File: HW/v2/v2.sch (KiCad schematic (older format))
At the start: 19 parts, among them J1 Encoder and LCD interface, J2 Fan_conn, J3 SDcardHeader, J4 OUT2, J5 OUT2, Q1 BC847, Q2 BC847, Q3 IRF7341, U1 LM75

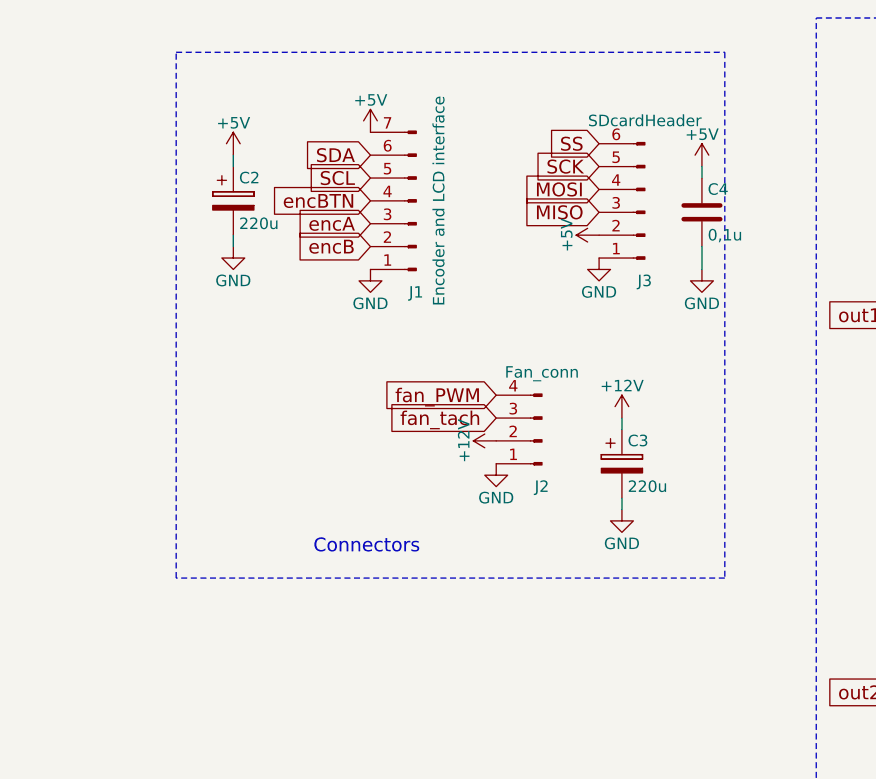
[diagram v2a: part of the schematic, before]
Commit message: i2c pots for calibrating
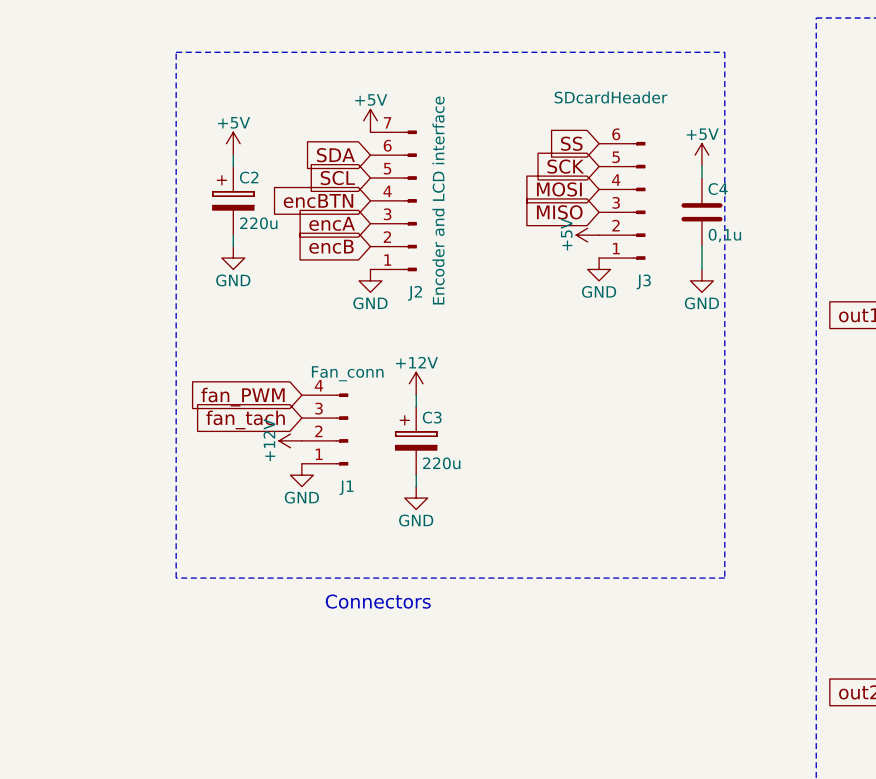
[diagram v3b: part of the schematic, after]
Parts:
- renumbered J2 to J1, J1 to J2
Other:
- moved on the sheet: C3, J1
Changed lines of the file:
@@
 encB
 $Comp
-L Conn_01x07_Male J1
+L Conn_01x07_Male J2
 U 1 1 5AD8A8D0
 P 6400 1600
-F 0 "J1" H 6400 2000 50  0000 C CNN
+F 0 "J2" H 6400 2000 50  0000 C CNN
 F 1 "Encoder and LCD interface" V 6300 1600 50  0000 C CNN
 F 2 "Pin_Headers:Pin_Header_Straight_1x07_Pitch2.54mm" H 6400 1600 50  0001 C CNN
@@
 	9950 3200 9950 3100
 Connection ~ 10250 3100
-Text GLabel 6750 2450 0    60   Input ~ 0
+Text GLabel 5900 2450 0    60   Input ~ 0
 fan_PWM
 $Comp
-L Conn_01x04_Male J2
+L Conn_01x04_Male J1
 U 1 1 5ADA285E
-P 6950 2650
-F 0 "J2" H 6950 2850 50  0000 C CNN
-F 1 "Fan_conn" H 6950 2350 50  0000 C CNN
-F 2 "Pin_Headers:Pin_Header_Straight_1x04_Pitch2.54mm" H 6950 2650 50  0001 C CNN
-F 3 "" H 6950 2650 50  0001 C CNN
-	1    6950 2650
+P 6100 2650
+F 0 "J1" H 6100 2850 50  0000 C CNN
+F 1 "Fan_conn" H 6100 2350 50  0000 C CNN
+F 2 "Pin_Headers:Pin_Header_Straight_1x04_Pitch2.54mm" H 6100 2650 50  0001 C CNN
+F 3 "" H 6100 2650 50  0001 C CNN
+	1    6100 2650
 	-1   0    0    1
 $EndComp
@@
 L +12V #PWR016
 U 1 1 5ADA2B19
-P 6750 2650
-F 0 "#PWR016" H 6750 2500 50  0001 C CNN
-F 1 "+12V" H 6750 2790 50  0000 C CNN
-F 2 "" H 6750 2650 50  0001 C CNN
-F 3 "" H 6750 2650 50  0001 C CNN
-	1    6750 2650
+P 5900 2650
+F 0 "#PWR016" H 5900 2500 50  0001 C CNN
+F 1 "+12V" H 5900 2790 50  0000 C CNN
+F 2 "" H 5900 2650 50  0001 C CNN
+F 3 "" H 5900 2650 50  0001 C CNN
+	1    5900 2650
 	0    -1   -1   0
 $EndComp
@@
 L GND #PWR017
 U 1 1 5ADA2C43
-P 6750 2750
-F 0 "#PWR017" H 6750 2500 50  0001 C CNN
-F 1 "GND" H 6750 2600 50  0000 C CNN
-F 2 "" H 6750 2750 50  0001 C CNN
-F 3 "" H 6750 2750 50  0001 C CNN
-	1    6750 2750
-	1    0    0    -1
-$EndComp
-Text GLabel 6750 2550 0    60   Input ~ 0
+P 5900 2750
+F 0 "#PWR017" H 5900 2500 50  0001 C CNN
+F 1 "GND" H 5900 2600 50  0000 C CNN
+F 2 "" H 5900 2750 50  0001 C CNN
+F 3 "" H 5900 2750 50  0001 C CNN
+	1    5900 2750
+	1    0    0    -1
+$EndComp
+Text GLabel 5900 2550 0    60   Input ~ 0
 fan_tach
 $Comp
@@
 P 7400 1650
 F 0 "J3" H 7400 1950 50  0000 C CNN
-F 1 "SDcardHeader" H 7400 1250 50  0000 C CNN
+F 1 "SDcardHeader" H 7550 1150 50  0000 C CNN
 F 2 "Pin_Headers:Pin_Header_Straight_1x06_Pitch2.54mm" H 7400 1650 50  0001 C CNN
 F 3 "" H 7400 1650 50  0001 C CNN
@@
 L CP C3
 U 1 1 5ADB1B22
-P 7300 2750
-F 0 "C3" H 7325 2850 50  0000 L CNN
-F 1 "220u" H 7325 2650 50  0000 L CNN
-F 2 "Capacitors_Tantalum_SMD:CP_Tantalum_Case-C_EIA-6032-28_Hand" H 7338 2600 50  0001 C CNN
-F 3 "" H 7300 2750 50  0001 C CNN
-	1    7300 2750
+P 6400 2650
+F 0 "C3" H 6425 2750 50  0000 L CNN
+F 1 "220u" H 6425 2550 50  0000 L CNN
+F 2 "Capacitors_Tantalum_SMD:CP_Tantalum_Case-C_EIA-6032-28_Hand" H 6438 2500 50  0001 C CNN
+F 3 "" H 6400 2650 50  0001 C CNN
+	1    6400 2650
 	1    0    0    -1
 $EndComp
@@
 L +12V #PWR022
 U 1 1 5ADB1BE0
-P 7300 2550
-F 0 "#PWR022" H 7300 2400 50  0001 C CNN
-F 1 "+12V" H 7300 2690 50  0000 C CNN
-F 2 "" H 7300 2550 50  0001 C CNN
-F 3 "" H 7300 2550 50  0001 C CNN
-	1    7300 2550
+P 6400 2450
+F 0 "#PWR022" H 6400 2300 50  0001 C CNN
+F 1 "+12V" H 6400 2590 50  0000 C CNN
+F 2 "" H 6400 2450 50  0001 C CNN
+F 3 "" H 6400 2450 50  0001 C CNN
+	1    6400 2450
 	1    0    0    -1
 $EndComp
@@
 L GND #PWR023
 U 1 1 5ADB1D03
-P 7300 2950
-F 0 "#PWR023" H 7300 2700 50  0001 C CNN
-F 1 "GND" H 7300 2800 50  0000 C CNN
-F 2 "" H 7300 2950 50  0001 C CNN
-F 3 "" H 7300 2950 50  0001 C CNN
-	1    7300 2950
-	1    0    0    -1
-$EndComp
-Wire Wire Line
-	7300 2900 7300 2950
-Wire Wire Line
-	7300 2600 7300 2550
+P 6400 2850
+F 0 "#PWR023" H 6400 2600 50  0001 C CNN
+F 1 "GND" H 6400 2700 50  0000 C CNN
+F 2 "" H 6400 2850 50  0001 C CNN
+F 3 "" H 6400 2850 50  0001 C CNN
+	1    6400 2850
+	1    0    0    -1
+$EndComp
+Wire Wire Line
+	6400 2800 6400 2850
+Wire Wire Line
+	6400 2500 6400 2450
 $Comp
 L CP C2
@@
 Wire Notes Line
 	5350 3250 5350 950
-Text Notes 5950 3150 0    60   ~ 0
+Text Notes 6000 3400 0    60   ~ 0
 Connectors
 $Sheet

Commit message: v2 done
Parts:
- removed D1, D2: D_ALT, Diodes_SMD:D_MELF-RM10_Universal_Handsoldering, symbol D_ALT
- removed J4, J5: OUT2, Pin_Headers:Pin_Header_Straight_1x02_Pitch2.54mm, symbol Conn_01x02
- removed Q1, Q2: BC847, TO_SOT_Packages_SMD:SOT-23_Handsoldering, symbol BC847
- removed Q3: IRF7341, Housings_SOIC:SOIC-8_3.9x4.9mm_Pitch1.27mm, symbol IRF7341
- removed R1, R2: 100R, Resistors_SMD:R_0805_HandSoldering, symbol R
- removed R3, R4: 10K, Resistors_SMD:R_0805_HandSoldering, symbol R
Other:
- note removed: "Generic outputs for Fan's/relay"

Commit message: more
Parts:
- C1, C4: symbol C -> device:C
- C2, C3: symbol CP -> device:CP
- J1: symbol Conn_01x04_Male -> conn:Conn_01x04_Male
- J2: symbol Conn_01x07_Male -> conn:Conn_01x07_Male
- J3: symbol Conn_01x06_Male -> conn:Conn_01x06_Male
- U1: symbol LM75 -> Peters:LM75
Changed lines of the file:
@@
-EESchema Schematic File Version 2
-LIBS:power
-LIBS:device
-LIBS:switches
-LIBS:relays
-LIBS:motors
-LIBS:transistors
-LIBS:conn
-LIBS:linear
-LIBS:regul
-LIBS:74xx
-LIBS:cmos4000
-LIBS:adc-dac
-LIBS:memory
-LIBS:xilinx
-LIBS:microcontrollers
-LIBS:dsp
-LIBS:microchip
-LIBS:analog_switches
-LIBS:motorola
-LIBS:texas
-LIBS:intel
-LIBS:audio
-LIBS:interface
-LIBS:digital-audio
-LIBS:philips
-LIBS:display
-LIBS:cypress
-LIBS:siliconi
-LIBS:opto
-LIBS:atmel
-LIBS:contrib
-LIBS:valves
-LIBS:Peters
-LIBS:BLUEPILL
+EESchema Schematic File Version 4
 LIBS:v2-cache
-EELAYER 25 0
+EELAYER 26 0
 EELAYER END
 $Descr A4 11693 8268
@@
 $EndDescr
 $Comp
-L LM75 U1
+L Peters:LM75 U1
 U 1 1 5AD8A8BE
 P 3250 6200
@@
 $EndComp
 $Comp
-L C C1
+L device:C C1
 U 1 1 5AD8A8BF
 P 1950 5700
@@
 $EndComp
 $Comp
-L GND #PWR01
+L power:GND #PWR01
 U 1 1 5AD8A8C0
 P 1950 5950
@@
 $EndComp
 $Comp
-L GND #PWR02
+L power:GND #PWR02
 U 1 1 5AD8A8C3
 P 3250 6650
@@
 encB
 $Comp
-L Conn_01x07_Male J2
+L conn:Conn_01x07_Male J2
 U 1 1 5AD8A8D0
 P 6400 1600
@@
 SDA
 $Comp
-L GND #PWR03
+L power:GND #PWR03
 U 1 1 5AD8A8D1
 P 6200 1900
@@
 $EndComp
 $Comp
-L +5V #PWR04
+L power:+5V #PWR04
 U 1 1 5AD8A8D2
 P 6200 1300
@@
 	3650 6100 3700 6100
 Wire Wire Line
-	3650 6300 4000 6300
+	3650 6300 3700 6300
 Wire Wire Line
 	4000 6300 4000 6400
@@
 	1950 5850 1950 5950
 $Comp
-L +5V #PWR013
+L power:+5V #PWR013
 U 1 1 5AD8A8F7
 P 3250 5750
@@
 $EndComp
 $Comp
-L +5V #PWR014
+L power:+5V #PWR014
 U 1 1 5AD8A8F8
 P 1950 5500
@@
 $EndComp
 $Comp
-L GND #PWR015
+L power:GND #PWR015
 U 1 1 5AD8A8F9
 P 4000 6400
@@
 	3650 6200 3700 6200
 Wire Wire Line
-	3700 6100 3700 6300
+	3700 6100 3700 6200
 Connection ~ 3700 6300
 Connection ~ 3700 6200
@@
 fan_PWM
 $Comp
-L Conn_01x04_Male J1
+L conn:Conn_01x04_Male J1
 U 1 1 5ADA285E
 P 6100 2650
@@
 $EndComp
 $Comp
-L +12V #PWR016
+L power:+12V #PWR016
 U 1 1 5ADA2B19
 P 5900 2650
@@
 $EndComp
 $Comp
-L GND #PWR017
+L power:GND #PWR017
 U 1 1 5ADA2C43
 P 5900 2750
@@
 fan_tach
 $Comp
-L Conn_01x06_Male J3
+L conn:Conn_01x06_Male J3
 U 1 1 5ADA41A2
 P 7400 1650
@@
 MOSI
 $Comp
-L C C4
+L device:C C4
 U 1 1 5ADA4B5E
 P 7650 1650
@@
 $EndComp
 $Comp
-L GND #PWR018
+L power:GND #PWR018
 U 1 1 5ADA4B64
 P 7650 1900
@@
 	7650 1800 7650 1900
 $Comp
-L +5V #PWR019
+L power:+5V #PWR019
 U 1 1 5ADA4B6C
 P 7650 1450
@@
 $EndComp
 $Comp
-L +5V #PWR020
+L power:+5V #PWR020
 U 1 1 5ADA5188
 P 7200 1750
@@
 $EndComp
 $Comp
-L GND #PWR021
+L power:GND #PWR021
 U 1 1 5ADA5217
 P 7200 1850
@@
 $EndComp
 $Comp
-L CP C3
+L device:CP C3
 U 1 1 5ADB1B22
 P 6400 2650
@@
 $EndComp
 $Comp
-L +12V #PWR022
+L power:+12V #PWR022
 U 1 1 5ADB1BE0
 P 6400 2450
@@
 $EndComp
 $Comp
-L GND #PWR023
+L power:GND #PWR023
 U 1 1 5ADB1D03
 P 6400 2850
@@
 	6400 2500 6400 2450
 $Comp
-L CP C2
+L device:CP C2
 U 1 1 5ADB20C3
 P 5600 1600
@@
 $EndComp
 $Comp
-L GND #PWR024
+L power:GND #PWR024
 U 1 1 5ADB20CF
 P 5600 1800
@@
 	5600 1450 5600 1400
 $Comp
-L +5V #PWR025
+L power:+5V #PWR025
 U 1 1 5ADB21EC
 P 5600 1400
@@
 F1 "file5AD8A8B3.sch" 60
 $EndSheet
+Wire Wire Line
+	3700 6300 4000 6300
+Wire Wire Line
+	3700 6200 3700 6300
 $EndSCHEMATC
